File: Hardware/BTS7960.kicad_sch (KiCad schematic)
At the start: 25 parts, among them J4 Screw_Terminal_01x04, U7 HCPL-2631, U8 HCPL-2631

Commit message: Update Sche
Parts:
- removed U5: ~, IVS_FOOTPRINTS:TO-263-7_TabPin8, symbol IVS_SYMBOLS:BTS7960
- added F3, F4: 30V/1.1A, Fuse:Fuse_Bourns_MF-RG300, symbol IVS_SYMBOLS:Fuse
- added U1: ~, symbol IVS_SYMBOLS:BTS7960
- J4: footprint (none) -> TerminalBlock:TerminalBlock_bornier-4_P5.08mm
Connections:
- net +24V_CS: now also F3.1, F4.1; no longer U2.7 (VS), U4.7 (VS), U6.7 (VS)
- net +5V_CS: now also U1.3 (INH)
- net GNDD: now also U1.1 (GND); no longer U7.2 (C1), U7.3 (C2), U8.2 (C1), U8.3 (C2)
- net Motor1: now also U1.4 (OUT), U1.8 (TAB)
- net PWM_DC_1: now also U1.2 (IN)
- net at R14.1: now also U1.6 (IS)
- net at R12.1: now also U1.5 (SR)
- new net +24V_M1: F3.2, U1.7 (VS), U6.7 (VS)
- new net +24V_M2: F4.2, U2.7 (VS), U4.7 (VS)
- new net GND: U7.2 (C1), U7.3 (C2), U8.2 (C1), U8.3 (C2)

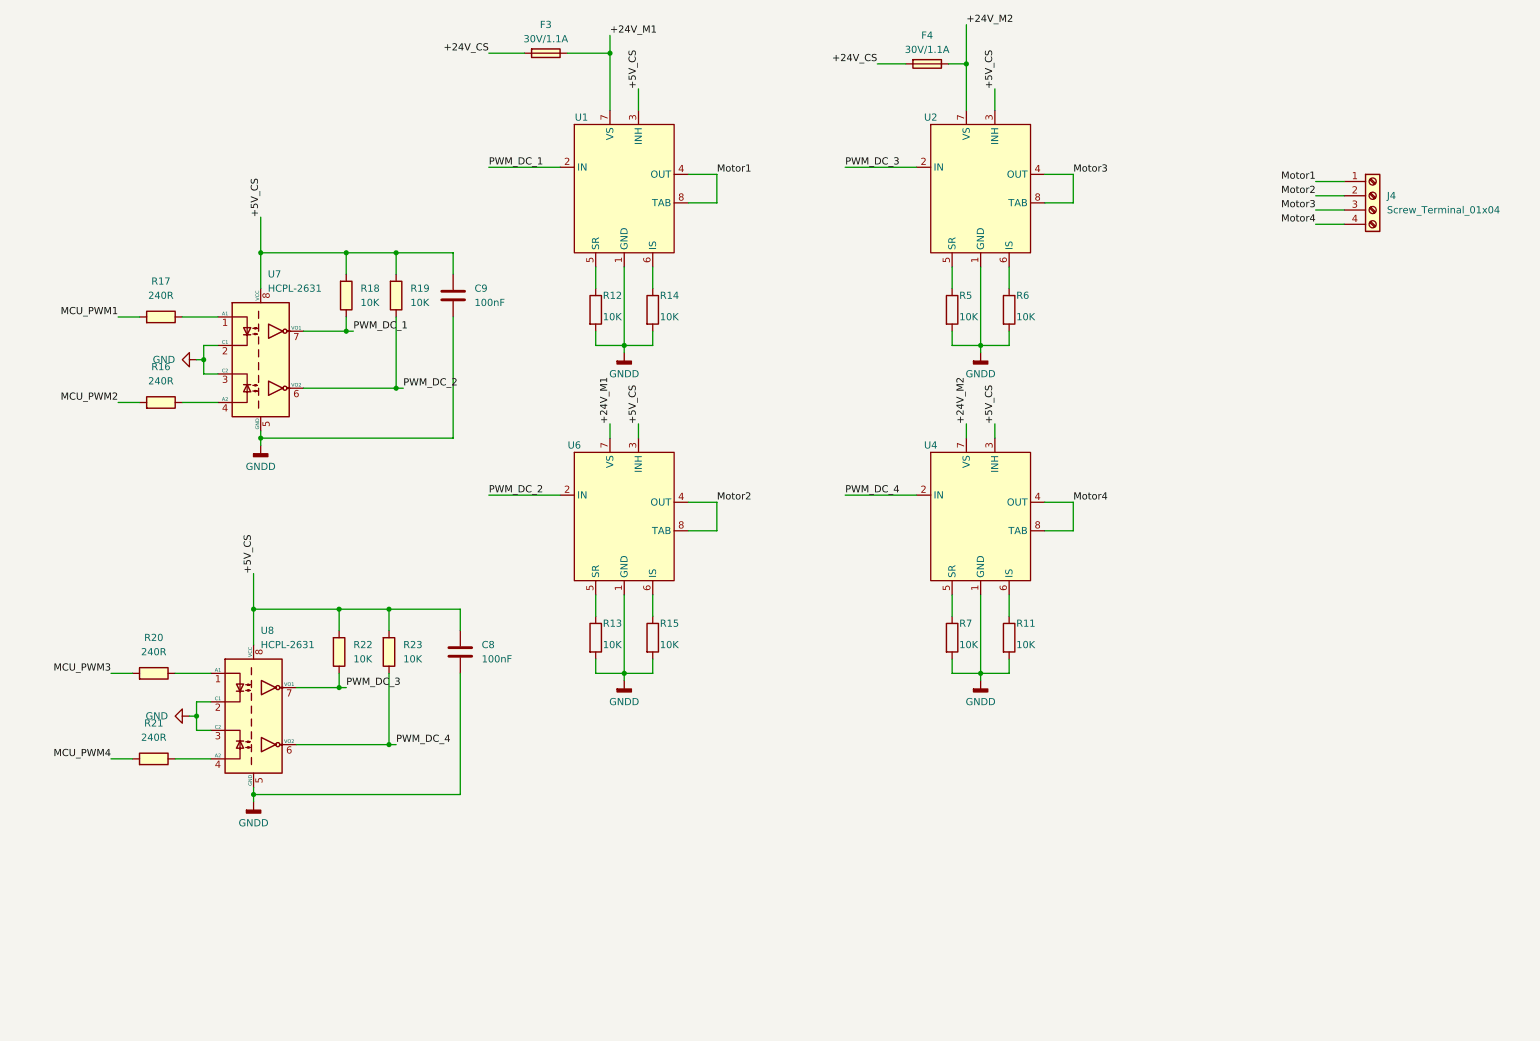
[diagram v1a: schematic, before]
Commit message: Hie BTS, fix GND opto MCT
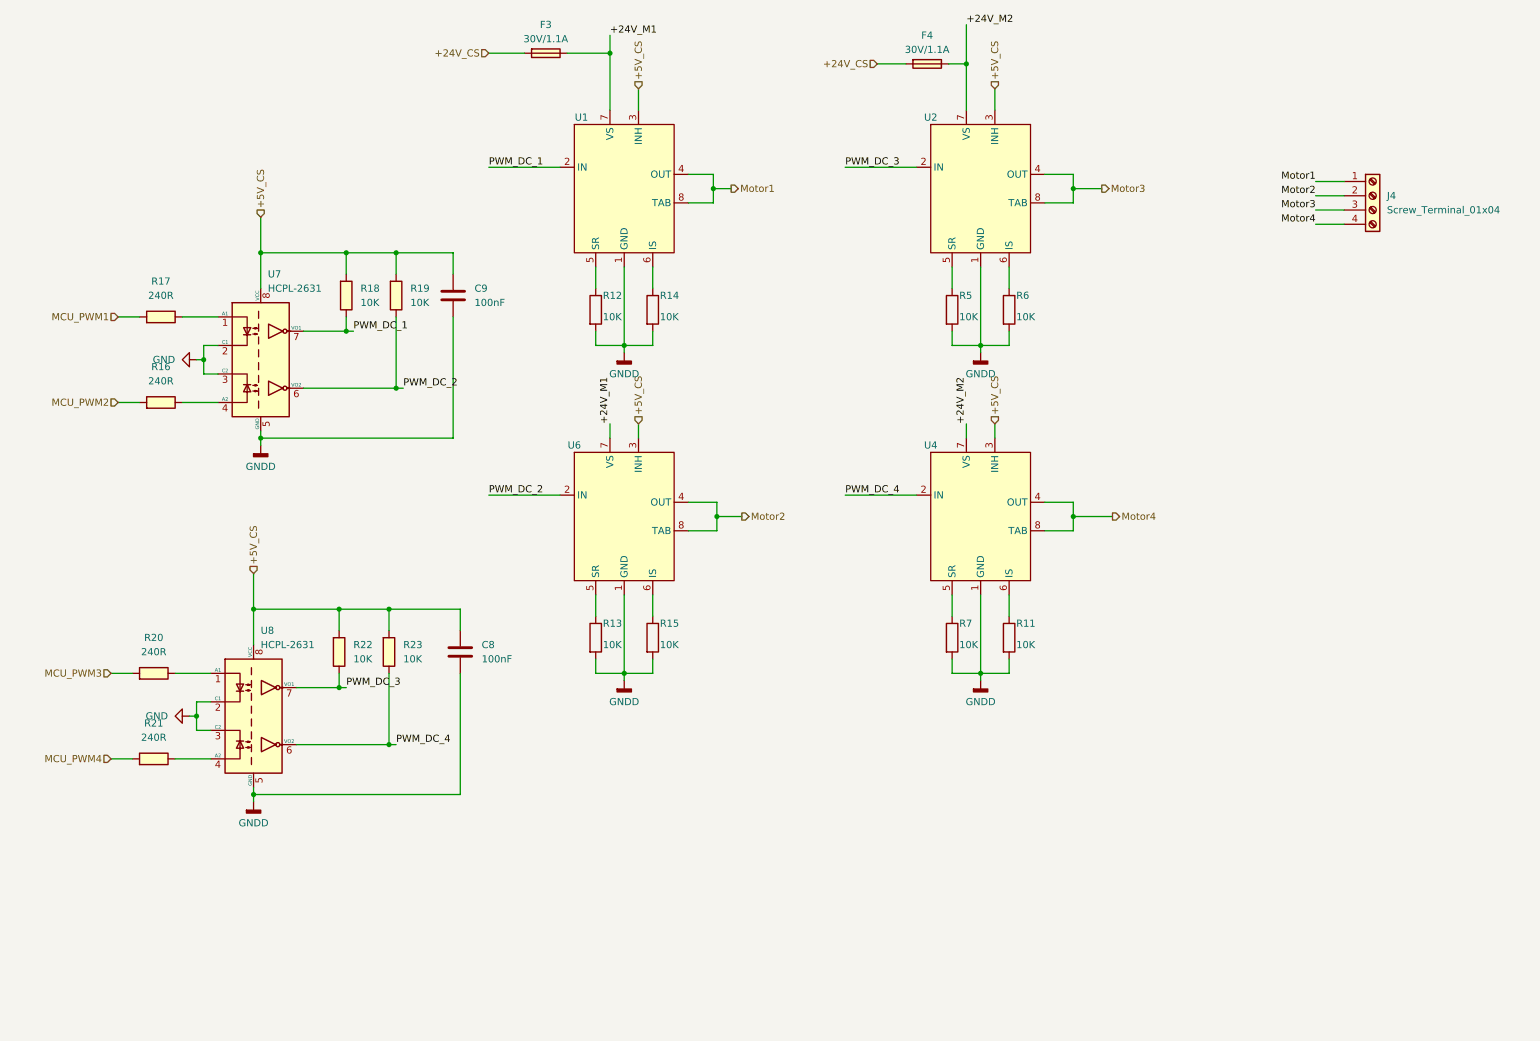
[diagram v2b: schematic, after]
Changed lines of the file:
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@@
   (junction (at 83.82 80.01) (diameter 0) (color 0 0 0 0)
   )
+  (junction (at 204.47 102.87) (diameter 0) (color 0 0 0 0)
+  )
   (junction (at 187.96 72.39) (diameter 0) (color 0 0 0 0)
   )
@@
   (junction (at 48.26 138.43) (diameter 0) (color 0 0 0 0)
   )
+  (junction (at 140.97 102.87) (diameter 0) (color 0 0 0 0)
+  )
   (junction (at 73.66 119.38) (diameter 0) (color 0 0 0 0)
   )
   (junction (at 58.42 119.38) (diameter 0) (color 0 0 0 0)
   )
+  (junction (at 140.335 44.45) (diameter 0) (color 0 0 0 0)
+  )
+  (junction (at 204.47 44.45) (diameter 0) (color 0 0 0 0)
+  )
   (junction (at 187.96 130.81) (diameter 0) (color 0 0 0 0)
   )
@@
     (stroke (width 0) (type default))
   )
+  (wire (pts (xy 140.335 44.45) (xy 143.51 44.45))
+    (stroke (width 0) (type default))
+  )
   (wire (pts (xy 82.55 143.51) (xy 83.82 143.51))
     (stroke (width 0) (type default))
@@
     (stroke (width 0) (type default))
   )
-  (wire (pts (xy 204.47 46.99) (xy 204.47 41.91))
+  (wire (pts (xy 204.47 46.99) (xy 204.47 44.45))
     (stroke (width 0) (type default))
   )
@@
     (stroke (width 0) (type default))
   )
+  (wire (pts (xy 204.47 102.87) (xy 211.455 102.87))
+    (stroke (width 0) (type default))
+  )
   (wire (pts (xy 46.99 138.43) (xy 48.26 138.43))
     (stroke (width 0) (type default))
@@
     (stroke (width 0) (type default))
   )
-  (wire (pts (xy 140.97 105.41) (xy 140.97 100.33))
+  (wire (pts (xy 140.97 105.41) (xy 140.97 102.87))
     (stroke (width 0) (type default))
   )
@@
     (stroke (width 0) (type default))
   )
-  (wire (pts (xy 135.89 46.99) (xy 140.97 46.99))
+  (wire (pts (xy 135.89 46.99) (xy 140.335 46.99))
     (stroke (width 0) (type default))
   )
@@
     (stroke (width 0) (type default))
   )
+  (wire (pts (xy 140.335 44.45) (xy 140.335 46.99))
+    (stroke (width 0) (type default))
+  )
   (wire (pts (xy 74.93 69.85) (xy 74.93 67.31))
     (stroke (width 0) (type default))
   )
-  (wire (pts (xy 135.89 41.91) (xy 140.97 41.91))
-    (stroke (width 0) (type default))
-  )
   (wire (pts (xy 119.38 128.27) (xy 119.38 130.81))
     (stroke (width 0) (type default))
@@
     (stroke (width 0) (type default))
   )
-  (wire (pts (xy 204.47 105.41) (xy 204.47 100.33))
+  (wire (pts (xy 204.47 105.41) (xy 204.47 102.87))
     (stroke (width 0) (type default))
   )
@@
     (stroke (width 0) (type default))
   )
+  (wire (pts (xy 204.47 44.45) (xy 209.55 44.45))
+    (stroke (width 0) (type default))
+  )
   (wire (pts (xy 129.54 58.42) (xy 129.54 62.23))
     (stroke (width 0) (type default))
@@
     (stroke (width 0) (type default))
   )
+  (wire (pts (xy 204.47 102.87) (xy 204.47 100.33))
+    (stroke (width 0) (type default))
+  )
   (wire (pts (xy 66.04 133.35) (xy 73.66 133.35))
     (stroke (width 0) (type default))
@@
     (stroke (width 0) (type default))
   )
+  (wire (pts (xy 140.335 41.91) (xy 135.89 41.91))
+    (stroke (width 0) (type default))
+  )
   (wire (pts (xy 49.53 74.93) (xy 49.53 77.47))
     (stroke (width 0) (type default))
@@
     (stroke (width 0) (type default))
   )
+  (wire (pts (xy 140.97 102.87) (xy 145.415 102.87))
+    (stroke (width 0) (type default))
+  )
   (wire (pts (xy 182.88 69.85) (xy 182.88 72.39))
     (stroke (width 0) (type default))
@@
     (stroke (width 0) (type default))
   )
+  (wire (pts (xy 204.47 44.45) (xy 204.47 41.91))
+    (stroke (width 0) (type default))
+  )
+  (wire (pts (xy 140.97 102.87) (xy 140.97 100.33))
+    (stroke (width 0) (type default))
+  )
   (wire (pts (xy 187.96 130.81) (xy 187.96 132.08))
     (stroke (width 0) (type default))
@@
     (stroke (width 0) (type default))
   )
-  (wire (pts (xy 140.97 46.99) (xy 140.97 41.91))
-    (stroke (width 0) (type default))
-  )
   (wire (pts (xy 182.88 72.39) (xy 187.96 72.39))
     (stroke (width 0) (type default))
@@
   )
   (wire (pts (xy 193.04 130.81) (xy 193.04 128.27))
+    (stroke (width 0) (type default))
+  )
+  (wire (pts (xy 140.335 41.91) (xy 140.335 44.45))
     (stroke (width 0) (type default))
   )
@@
     (effects (font (size 1.27 1.27)) (justify left bottom))
   )
-  (label "Motor2" (at 140.97 100.33 0) (fields_autoplaced)
-    (effects (font (size 1.27 1.27)) (justify left bottom))
-  )
   (label "PWM_DC_1" (at 100.33 40.64 0) (fields_autoplaced)
     (effects (font (size 1.27 1.27)) (justify left bottom))
@@
     (effects (font (size 1.27 1.27)) (justify left bottom))
   )
-  (label "Motor1" (at 140.97 41.91 0) (fields_autoplaced)
-    (effects (font (size 1.27 1.27)) (justify left bottom))
-  )
-  (label "+24V_CS" (at 169.545 22.225 180) (fields_autoplaced)
-    (effects (font (size 1.27 1.27)) (justify right bottom))
-  )
   (label "PWM_DC_3" (at 74.93 133.35 0) (fields_autoplaced)
     (effects (font (size 1.27 1.27)) (justify left bottom))
-  )
-  (label "MCU_PWM3" (at 33.02 130.81 180) (fields_autoplaced)
-    (effects (font (size 1.27 1.27)) (justify right bottom))
-  )
-  (label "MCU_PWM4" (at 33.02 146.05 180) (fields_autoplaced)
-    (effects (font (size 1.27 1.27)) (justify right bottom))
   )
   (label "Motor2" (at 247.65 45.72 180) (fields_autoplaced)
     (effects (font (size 1.27 1.27)) (justify right bottom))
   )
-  (label "Motor4" (at 204.47 100.33 0) (fields_autoplaced)
-    (effects (font (size 1.27 1.27)) (justify left bottom))
-  )
-  (label "+5V_CS" (at 59.69 49.53 90) (fields_autoplaced)
-    (effects (font (size 1.27 1.27)) (justify left bottom))
-  )
-  (label "Motor3" (at 204.47 41.91 0) (fields_autoplaced)
-    (effects (font (size 1.27 1.27)) (justify left bottom))
-  )
   (label "PWM_DC_1" (at 76.2 69.85 0) (fields_autoplaced)
     (effects (font (size 1.27 1.27)) (justify left bottom))
@@
     (effects (font (size 1.27 1.27)) (justify left bottom))
   )
-  (label "+24V_CS" (at 100.33 20.32 180) (fields_autoplaced)
-    (effects (font (size 1.27 1.27)) (justify right bottom))
-  )
-  (label "+5V_CS" (at 58.42 113.03 90) (fields_autoplaced)
-    (effects (font (size 1.27 1.27)) (justify left bottom))
-  )
   (label "Motor4" (at 247.65 50.8 180) (fields_autoplaced)
     (effects (font (size 1.27 1.27)) (justify right bottom))
   )
-  (label "MCU_PWM1" (at 34.29 67.31 180) (fields_autoplaced)
-    (effects (font (size 1.27 1.27)) (justify right bottom))
-  )
   (label "+24V_M1" (at 121.92 86.36 90) (fields_autoplaced)
     (effects (font (size 1.27 1.27)) (justify left bottom))
@@
     (effects (font (size 1.27 1.27)) (justify left bottom))
   )
-  (label "+5V_CS" (at 127 86.36 90) (fields_autoplaced)
-    (effects (font (size 1.27 1.27)) (justify left bottom))
-  )
-  (label "+5V_CS" (at 190.5 86.36 90) (fields_autoplaced)
-    (effects (font (size 1.27 1.27)) (justify left bottom))
-  )
-  (label "+5V_CS" (at 190.5 26.67 90) (fields_autoplaced)
-    (effects (font (size 1.27 1.27)) (justify left bottom))
-  )
-  (label "+5V_CS" (at 127 26.67 90) (fields_autoplaced)
-    (effects (font (size 1.27 1.27)) (justify left bottom))
-  )
-  (label "MCU_PWM2" (at 34.29 82.55 180) (fields_autoplaced)
-    (effects (font (size 1.27 1.27)) (justify right bottom))
-  )
   (label "PWM_DC_2" (at 100.33 99.06 0) (fields_autoplaced)
     (effects (font (size 1.27 1.27)) (justify left bottom))
   )
+  (hierarchical_label "Motor2" (shape output) (at 145.415 102.87 0) (fields_autoplaced)
+    (effects (font (size 1.27 1.27)) (justify left))
+  )
+  (hierarchical_label "+24V_CS" (shape input) (at 169.545 22.225 180) (fields_autoplaced)
+    (effects (font (size 1.27 1.27)) (justify right))
+  )
+  (hierarchical_label "+5V_CS" (shape input) (at 127 86.36 90) (fields_autoplaced)
+    (effects (font (size 1.27 1.27)) (justify left))
+  )
+  (hierarchical_label "+5V_CS" (shape input) (at 127 26.67 90) (fields_autoplaced)
+    (effects (font (size 1.27 1.27)) (justify left))
+  )
+  (hierarchical_label "Motor3" (shape output) (at 209.55 44.45 0) (fields_autoplaced)
+    (effects (font (size 1.27 1.27)) (justify left))
+  )
+  (hierarchical_label "+5V_CS" (shape input) (at 190.5 26.67 90) (fields_autoplaced)
+    (effects (font (size 1.27 1.27)) (justify left))
+  )
+  (hierarchical_label "MCU_PWM4" (shape input) (at 33.02 146.05 180) (fields_autoplaced)
+    (effects (font (size 1.27 1.27)) (justify right))
+  )
+  (hierarchical_label "+5V_CS" (shape input) (at 59.69 49.53 90) (fields_autoplaced)
+    (effects (font (size 1.27 1.27)) (justify left))
+  )
+  (hierarchical_label "+5V_CS" (shape input) (at 190.5 86.36 90) (fields_autoplaced)
+    (effects (font (size 1.27 1.27)) (justify left))
+  )
+  (hierarchical_label "+5V_CS" (shape input) (at 58.42 113.03 90) (fields_autoplaced)
+    (effects (font (size 1.27 1.27)) (justify left))
+  )
+  (hierarchical_label "MCU_PWM3" (shape input) (at 33.02 130.81 180) (fields_autoplaced)
+    (effects (font (size 1.27 1.27)) (justify right))
+  )
+  (hierarchical_label "+24V_CS" (shape input) (at 100.33 20.32 180) (fields_autoplaced)
+    (effects (font (size 1.27 1.27)) (justify right))
+  )
+  (hierarchical_label "Motor1" (shape output) (at 143.51 44.45 0) (fields_autoplaced)
+    (effects (font (size 1.27 1.27)) (justify left))
+  )
+  (hierarchical_label "MCU_PWM2" (shape input) (at 34.29 82.55 180) (fields_autoplaced)
+    (effects (font (size 1.27 1.27)) (justify right))
+  )
+  (hierarchical_label "Motor4" (shape output) (at 211.455 102.87 0) (fields_autoplaced)
+    (effects (font (size 1.27 1.27)) (justify left))
+  )
+  (hierarchical_label "MCU_PWM1" (shape input) (at 34.29 67.31 180) (fields_autoplaced)
+    (effects (font (size 1.27 1.27)) (justify right))
+  )
   (symbol (lib_id "IVS_SYMBOLS:R") (at 40.64 146.05 90) (unit 1)

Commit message: Up schematic
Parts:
- added J10, J11: Screw_Terminal_01x04, Connector_PinHeader_2.54mm:PinHeader_1x04_P2.54mm_Vertical, symbol Connector:Screw_Terminal_01x04
- U1: footprint (none) -> IVS_FOOTPRINTS:TO-263-7_TabPin8
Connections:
- net +5V_CS: now also J10.3 (Pin_3), J11.3 (Pin_3)
- net GNDD: now also J10.4 (Pin_4), J11.4 (Pin_4)
- net MCU_PWM1 renamed MCU_PWM_L1
- net MCU_PWM2 renamed MCU_PWM_R1
- net MCU_PWM3 renamed MCU_PWM_L2
- net MCU_PWM4 renamed MCU_PWM_R2
- net Motor1 renamed Motor_L1
- net Motor2 renamed Motor_R1
- net Motor3 renamed Motor_L2
- net Motor4 renamed Motor_R2
- net PWM_DC_1 renamed PWM_DC_L1
- net PWM_DC_2 renamed PWM_DC_R1
- net PWM_DC_3 renamed PWM_DC_L2
- net PWM_DC_4 renamed PWM_DC_R2
- new net EnA_1: J10.2 (Pin_2)
- new net EnA_2: J11.2 (Pin_2)
- new net EnB_1: J10.1 (Pin_1)
- new net EnB_2: J11.1 (Pin_1)
